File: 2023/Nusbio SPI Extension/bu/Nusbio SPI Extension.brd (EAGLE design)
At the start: 54 x 65 mm, 12 parts

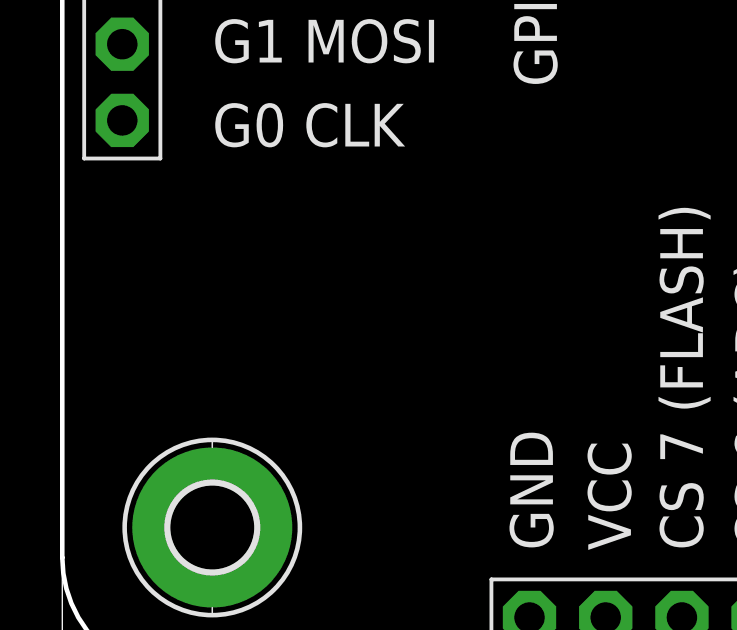
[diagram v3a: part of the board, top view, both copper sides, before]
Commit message: Finishh and send board for summer 2023 to jlpcb
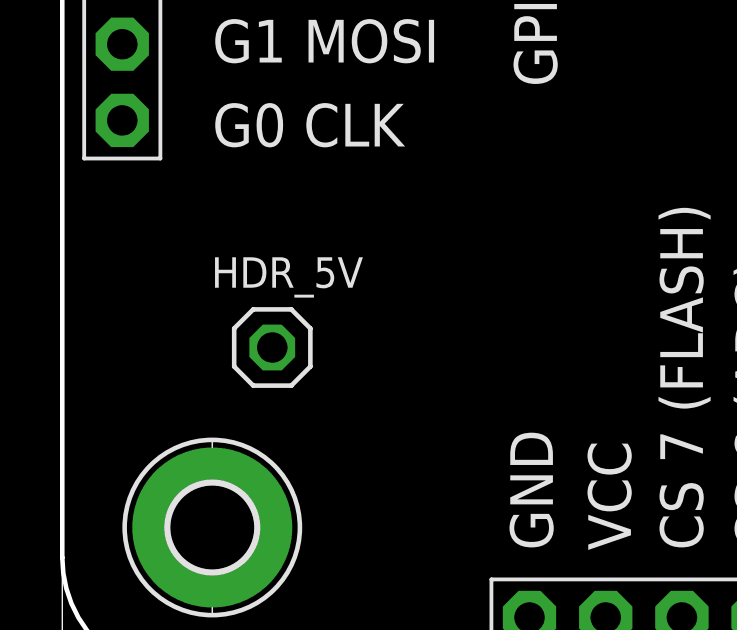
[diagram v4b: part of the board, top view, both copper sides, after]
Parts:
- added HDR_5V: (no value), pinhead:1X01
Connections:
- new net VCC_5V: HDR_5V.1, MCP_3008_3_3V.16
- net VCC: no longer MCP_3008_3_3V.16
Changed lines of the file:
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@@
 <attribute name="POPULARITY" value="6" x="49" y="5" size="1.778" layer="27" display="off"/>
+</element>
+<element name="HDR_5V" library="pinhead" library_urn="urn:adsk.eagle:library:325" package="1X01" package3d_urn="urn:adsk.eagle:package:22485/2" value="" x="7" y="11" smashed="yes">
+<attribute name="NAME" x="7.5" y="13.5" size="1.016" layer="25" ratio="10" align="center"/>
+<attribute name="POPULARITY" value="64" x="7" y="11" size="1.778" layer="27" display="off"/>
+<attribute name="VALUE" x="5.73" y="7.825" size="1.27" layer="27"/>
 </element>
 </elements>
@@
 <contactref element="SOIC8_208MIL" pad="7"/>
 <contactref element="ADC_IN_3_3V" pad="9"/>
-<contactref element="MCP_3008_3_3V" pad="16"/>
 <contactref element="MCP_3008_3_3V" pad="15"/>
-<wire x1="37.455" y1="41.445" x2="35.89" y2="63" width="0" layer="19" extent="1-1"/>
-<wire x1="37.455" y1="40.175" x2="37.455" y2="41.445" width="0" layer="19" extent="1-1"/>
-<wire x1="24.815" y1="41.405" x2="37.455" y2="41.445" width="0" layer="19" extent="1-1"/>
-<wire x1="24.815" y1="40.135" x2="24.815" y2="41.405" width="0" layer="19" extent="1-1"/>
+<wire x1="37.455" y1="40.175" x2="35.89" y2="63" width="0" layer="19" extent="1-1"/>
+<wire x1="24.815" y1="40.135" x2="37.455" y2="40.175" width="0" layer="19" extent="1-1"/>
+<wire x1="24.815" y1="41.405" x2="24.815" y2="40.135" width="0" layer="19" extent="1-1"/>
 <wire x1="18.185" y1="38.865" x2="24.815" y2="40.135" width="0" layer="19" extent="1-1"/>
-<wire x1="2" y1="38.89" x2="18.185" y2="38.865" width="0" layer="19" extent="1-1"/>
 <wire x1="52" y1="39.11" x2="37.455" y2="40.175" width="0" layer="19" extent="1-1"/>
 <wire x1="28.8398" y1="25.4567" x2="24.815" y2="40.135" width="0" layer="19" extent="1-1"/>
+<wire x1="2" y1="38.89" x2="18.185" y2="38.865" width="0" layer="19" extent="1-1"/>
 <wire x1="18.114771875" y1="2" x2="28.8398" y2="25.4567" width="0" layer="19" extent="1-1"/>
-<wire x1="52" y1="13.11" x2="28.8398" y2="25.4567" width="0" layer="19" extent="1-1"/>
+<wire x1="52" y1="13.11" x2="52" y2="39.11" width="0" layer="19" extent="1-1"/>
 </signal>
 <signal name="GPIO6">
@@
 <wire x1="32.545" y1="32.555" x2="52" y2="41.65" width="0" layer="19" extent="1-1"/>
 </signal>
+<signal name="VCC_5V">
+<contactref element="MCP_3008_3_3V" pad="16"/>
+<contactref element="HDR_5V" pad="1"/>
+<wire x1="7" y1="11" x2="37.455" y2="41.445" width="0" layer="19" extent="1-1"/>
+</signal>
 </signals>
